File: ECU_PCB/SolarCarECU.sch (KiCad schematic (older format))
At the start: 123 parts, among them J1 Screw_Terminal_01x02, J2 USB_B, J3 Screw_Terminal_01x05, J4 Screw_Terminal_01x08, J5 Screw_Terminal_01x08, J6 Screw_Terminal_01x14, J7 Screw_Terminal_01x14, Q1 QM6015D, Q2 PZT2222A, Q3 QM6015D, Q4 QM6015D, Q5 QM6015D, Q6 QM6015D, U1 Teensy3.6, U10 LM324A, U2 EL7202CN, U3 EL7202CN, U4 L7805, U5 MCP2562-E-P, U6 MCP2562-E-P, U7 4504, U8 4504, U9 4504

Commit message: fixed UART_1_* pins, added LV_KILL_SENSE, added *STEER_CTRL*
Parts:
- added C41: C, Capacitor_SMD:C_0603_1608Metric, symbol SolarCarECU-rescue:C-Device-SolarCarECU-rescue
- added D10, D3, D4, D5, D6, D7, D8, D9: D, Diode_SMD:D_SOD-123, symbol Device:D
- added R58, R59: R, Resistor_SMD:R_0603_1608Metric, symbol SolarCarECU-rescue:R-Device-SolarCarECU-rescue
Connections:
- net labels added: LV_STEER_CTRL, STEER_CTRL
- net labels removed: UART_RX, UART_TX
- wire segments 576 -> 618
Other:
- moved on the sheet: C21, C30, C35, C37, C38, C39, C40, R12, R13, R18, R19, R28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

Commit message: reworked PCB and fixed all issues brought up
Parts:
- removed BT1: Battery_Cell, Battery:BatteryHolder_Keystone_1060_1x2032, symbol Device:Battery_Cell
- removed C4: 470uF, Capacitor_THT:CP_Radial_D13.0mm_P5.00mm, symbol SolarCarECU-rescue:CP-Device-SolarCarECU-rescue
- removed D1: D_Schottky, Diode_SMD:D_SOD-123, symbol SolarCarECU-rescue:D_Schottky-Device-SolarCarECU-rescue
- removed D2: D_Zener, Diode_SMD:D_SOD-123, symbol SolarCarECU-rescue:D_Zener-Device-SolarCarECU-rescue
- removed J1: Screw_Terminal_01x02, Connector_Phoenix_MC_HighVoltage:PhoenixContact_MCV_1,5_2-G-5.08_1x02_P5.08mm_Vertical, symbol SolarCarECU-rescue:Screw_Terminal_01x02-Connector-SolarCarECU-rescue
- removed J2: USB_B, Connector_USB:USB_B_OST_USB-B1HSxx_Horizontal, symbol Connector:USB_B
- removed J3: Screw_Terminal_01x05, Connector_Phoenix_MC_HighVoltage:PhoenixContact_MCV_1,5_5-G-5.08_1x05_P5.08mm_Vertical, symbol Connector:Screw_Terminal_01x05
- removed J4, J5: Screw_Terminal_01x08, Connector_PinSocket_2.54mm:PinSocket_1x08_P2.54mm_Vertical, symbol SolarCarECU-rescue:Screw_Terminal_01x08-Connector-SolarCarECU-rescue
- removed J6, J7: Screw_Terminal_01x14, Connector_PinSocket_2.54mm:PinSocket_1x14_P2.54mm_Vertical, symbol SolarCarECU-rescue:Screw_Terminal_01x14-Connector-SolarCarECU-rescue
- removed Q2: PZT2222A, Package_TO_SOT_SMD:SOT-223, symbol SolarCarECU-rescue:PZT2222A-Transistor_BJT-SolarCarECU-rescue
- removed R43: 0, Resistor_SMD:R_1206_3216Metric, symbol SolarCarECU-rescue:R-Device-SolarCarECU-rescue
- removed R7: 120, Resistor_SMD:R_0603_1608Metric, symbol SolarCarECU-rescue:R-Device-SolarCarECU-rescue
- added C2: 470uF, Capacitor_THT:CP_Radial_D13.0mm_P5.00mm, symbol SolarCarECU-rescue:CP-Device-SolarCarECU-rescue
- added C7: 100n, Capacitor_SMD:C_1206_3216Metric, symbol SolarCarECU-rescue:C-Device-SolarCarECU-rescue
- added C8: 4.7u, Capacitor_SMD:C_1206_3216Metric, symbol SolarCarECU-rescue:C-Device-SolarCarECU-rescue
- added D1: 599-0210, LED_SMD:LED_1206_3216Metric, symbol Device:LED
- added D12, D13, D6, D7: D, Diode_SMD:D_SOD-123, symbol SolarCarECU-rescue:D-Device
- added D16: 599-0291, LED_SMD:LED_1206_3216Metric, symbol Device:LED
- added D2: D_Zener, Diode_SMD:D_SOD-123, symbol Device:D_Zener
- added D3: 599-0230, LED_SMD:LED_1206_3216Metric, symbol Device:LED
- added J2: Screw_Terminal_01x08, Connector_Phoenix_MC_HighVoltage:PhoenixContact_MCV_1,5_8-G-5.08_1x08_P5.08mm_Vertical, symbol Connector:Screw_Terminal_01x08
- added J3, J4, J5, J6, J7, J8: Screw_Terminal_01x08, Connector_PinSocket_2.54mm:PinSocket_1x08_P2.54mm_Vertical, symbol Connector:Screw_Terminal_01x08
- added Q4, Q5: QM6015D, Package_TO_SOT_SMD:TO-252-2, symbol SolarCarECU-rescue:QM6015D-Transistor_FET-SolarCarECU-rescue
- added R43, R7: 4.7, Resistor_SMD:R_0603_1608Metric, symbol SolarCarECU-rescue:R-Device
- added R6, R61, R62: 1k, Resistor_SMD:R_1206_3216Metric, symbol SolarCarECU-rescue:R-Device-SolarCarECU-rescue
- added U11: MCP1403, Package_DIP:DIP-8_W7.62mm, symbol SolarCarECU-rescue:EL7202CN-Driver_FET-SolarCarECU-rescue
- C10: renamed from C3; value 0.47u -> 100n; footprint Capacitor_SMD:C_0603_1608Metric -> Capacitor_SMD:C_1206_3216Metric
- C11: renamed from C6; footprint Capacitor_SMD:C_0603_1608Metric -> Capacitor_SMD:C_1206_3216Metric
- C12: renamed from C8; footprint Capacitor_SMD:C_0603_1608Metric -> Capacitor_SMD:C_1206_3216Metric
- C13: renamed from C11; value 0.47u -> 100n; footprint Capacitor_SMD:C_0603_1608Metric -> Capacitor_SMD:C_1206_3216Metric
- C14: renamed from C12; value 0.47u -> 100n; footprint Capacitor_SMD:C_0603_1608Metric -> Capacitor_SMD:C_1206_3216Metric
- C15: renamed from C13; value 0.47u -> 100n; footprint Capacitor_SMD:C_0603_1608Metric -> Capacitor_SMD:C_1206_3216Metric
- C16: renamed from C14; value 0.47u -> 100n; footprint Capacitor_SMD:C_0603_1608Metric -> Capacitor_SMD:C_1206_3216Metric
- C17: renamed from C15; value 0.47u -> 100n; footprint Capacitor_SMD:C_0603_1608Metric -> Capacitor_SMD:C_1206_3216Metric
- C18: renamed from C16; value 0.47u -> 100n; footprint Capacitor_SMD:C_0603_1608Metric -> Capacitor_SMD:C_1206_3216Metric
- C19: renamed from C17; value 0.47u -> 100n; footprint Capacitor_SMD:C_0603_1608Metric -> Capacitor_SMD:C_1206_3216Metric
- C20: renamed from C18; footprint Capacitor_SMD:C_0603_1608Metric -> Capacitor_SMD:C_1206_3216Metric
- C21, C30, C35, C37, C38, C39, C40, C41: value C -> 1n
- C3: renamed from C10; footprint Capacitor_THT:CP_Radial_D13.0mm_P5.00mm -> Capacitor_SMD:C_1206_3216Metric
- C36: renamed from C19; footprint Capacitor_SMD:C_0603_1608Metric -> Capacitor_SMD:C_1206_3216Metric
- C4: renamed from C2; value 0.47u -> 100n; footprint Capacitor_SMD:C_0603_1608Metric -> Capacitor_SMD:C_1206_3216Metric
- C42: renamed from C20; footprint Capacitor_SMD:C_0603_1608Metric -> Capacitor_SMD:C_1206_3216Metric
- C43: renamed from C36; value 0.47u -> 100n; footprint Capacitor_SMD:C_0603_1608Metric -> Capacitor_SMD:C_1206_3216Metric
- C5: footprint Capacitor_SMD:C_0603_1608Metric -> Capacitor_SMD:C_1206_3216Metric
- C6: renamed from C7; footprint Capacitor_SMD:C_0603_1608Metric -> Capacitor_SMD:C_1206_3216Metric
- C9: value 10uF -> 47u; footprint Capacitor_SMD:C_0603_1608Metric -> Capacitor_SMD:C_1206_3216Metric
- D10: renamed from D7; symbol Device:D -> SolarCarECU-rescue:D-Device
- D11: renamed from D8; symbol Device:D -> SolarCarECU-rescue:D-Device
- D14: renamed from D9; symbol Device:D -> SolarCarECU-rescue:D-Device
- D15: renamed from D10; symbol Device:D -> SolarCarECU-rescue:D-Device
- D4: renamed from D3; symbol Device:D -> SolarCarECU-rescue:D-Device
- D5: renamed from D4; symbol Device:D -> SolarCarECU-rescue:D-Device
- D8: renamed from D5; symbol Device:D -> SolarCarECU-rescue:D-Device
- D9: renamed from D6; symbol Device:D -> SolarCarECU-rescue:D-Device
- R1, R10, R11, R2, R3, R4, R52, R53, R8, R9: footprint Resistor_SMD:R_0603_1608Metric -> Resistor_SMD:R_1206_3216Metric
- R12, R18, R28, R30, R40, R44, R46, R58: value R -> 1M
- R13, R19, R29, R31, R41, R45, R47, R59: value R -> 330k
- R48, R49, R50, R51: symbol Device:R -> SolarCarECU-rescue:R-Device
- R60: renamed from R6; footprint Resistor_SMD:R_0603_1608Metric -> Resistor_SMD:R_1206_3216Metric
- U2, U3: value EL7202CN -> MCP1403
- renumbered Q3 to Q2, Q5 to Q3, Q4 to Q6, Q6 to Q7
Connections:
- net labels added: +VDC, LEFT_BLINKERS, LV_LEFT_BLINKERS, LV_RIGHT_BLINKERS, LV_STROBE, RIGHT_BLINKERS, STROBE
- net labels removed: BLINKERS, LV_BLINKERS, USB_MASTER-SLAVE_SEL
- wire segments 618 -> 663
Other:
- note removed: "This resistor is for debugging.\nIt can be removed it to disconnect\n12V from everything else."
- moved on the sheet: C1, C10, C11, C12, C13, C14, C15, C16, C17, C18, C19, C20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

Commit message: added HORN_CTRL and fixed silkscreen issues
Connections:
- net GND: no longer U7.14 (Fin)
- net HAZARD_LED: no longer J6.8 (Pin_8)
- net LV_HORN_CTRL: now reaches U1.49 (22_A8_PWM_Touch)
- net LV_HORN_CTRL: now also U7.15 (Fout)
- new net HORN_CTRL: J6.8 (Pin_8), U7.14 (Fin)
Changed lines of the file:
@@
 Wire Wire Line
 	10700 2600 11400 2600
-Wire Wire Line
-	10700 3000 10950 3000
 $Comp
 L SolarCarECU-rescue:+12V-power-SolarCarECU-rescue #PWR0139
@@
 Text Label 20450 7450 0    50   ~ 0
 KILL_SENSE
-Text Label 20450 7550 0    50   ~ 0
-HAZARD_LED
 Text Label 20450 3450 0    50   ~ 0
 BRAKELIGHTS
@@
 Connection ~ 3450 2700
 Wire Wire Line
-	10950 3200 10950 3000
-Connection ~ 10950 3200
-Wire Wire Line
 	21100 8200 21250 8200
 Text Label 20450 3250 0    50   ~ 0
@@
 Wire Wire Line
 	3450 1400 4150 1400
+Text Label 11400 3000 2    50   ~ 0
+HORN_CTRL
+Text Label 9700 3000 2    50   ~ 0
+LV_HORN_CTRL
+Wire Wire Line
+	9700 3000 9800 3000
+Text Label 5450 14250 0    50   ~ 0
+LV_HORN_CTRL
+Wire Wire Line
+	5400 14250 5450 14250
+Wire Wire Line
+	10700 3000 11400 3000
+Text Label 20450 7550 0    50   ~ 0
+HORN_CTRL
 $EndSCHEMATC

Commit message: added HEADLIGHT_CTRL pin but had to sacrifice a 12V output for it.
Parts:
- added C44: 1n, Capacitor_SMD:C_0603_1608Metric, symbol SolarCarECU-rescue:C-Device-SolarCarECU-rescue
- added R63: 1M, Resistor_SMD:R_0603_1608Metric, symbol SolarCarECU-rescue:R-Device-SolarCarECU-rescue
- added R64: 330k, Resistor_SMD:R_0603_1608Metric, symbol SolarCarECU-rescue:R-Device-SolarCarECU-rescue
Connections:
- net +12V: no longer J6.1 (Pin_1)
- net GNDA: now also J6.1 (Pin_1), C44.2, R64.2; no longer J6.2 (Pin_2)
- net LV_HEADLIGHT_CTRL: now reaches U1.50 (23_A9_PWM_Touch)
- net LV_HEADLIGHT_CTRL: now also C44.1, R63.2, R64.1
- new net HEADLIGHT_CTRL: J6.2 (Pin_2), R63.1
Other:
- moved on the sheet: R12, R18, R28, R30, R40, R44, R46, R58

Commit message: schema update
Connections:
- net LV_STROBE: now also U1.8 (6_PWM)
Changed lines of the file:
@@
 EESchema Schematic File Version 4
 LIBS:SolarCarECU-cache
-EELAYER 29 0
+EELAYER 26 0
 EELAYER END
 $Descr A2 23386 16535
@@
 Wire Wire Line
 	5400 14150 5450 14150
+Text Label 2900 11250 2    50   ~ 0
+LV_STROBE
+Wire Wire Line
+	2900 11250 3400 11250
 $EndSCHEMATC

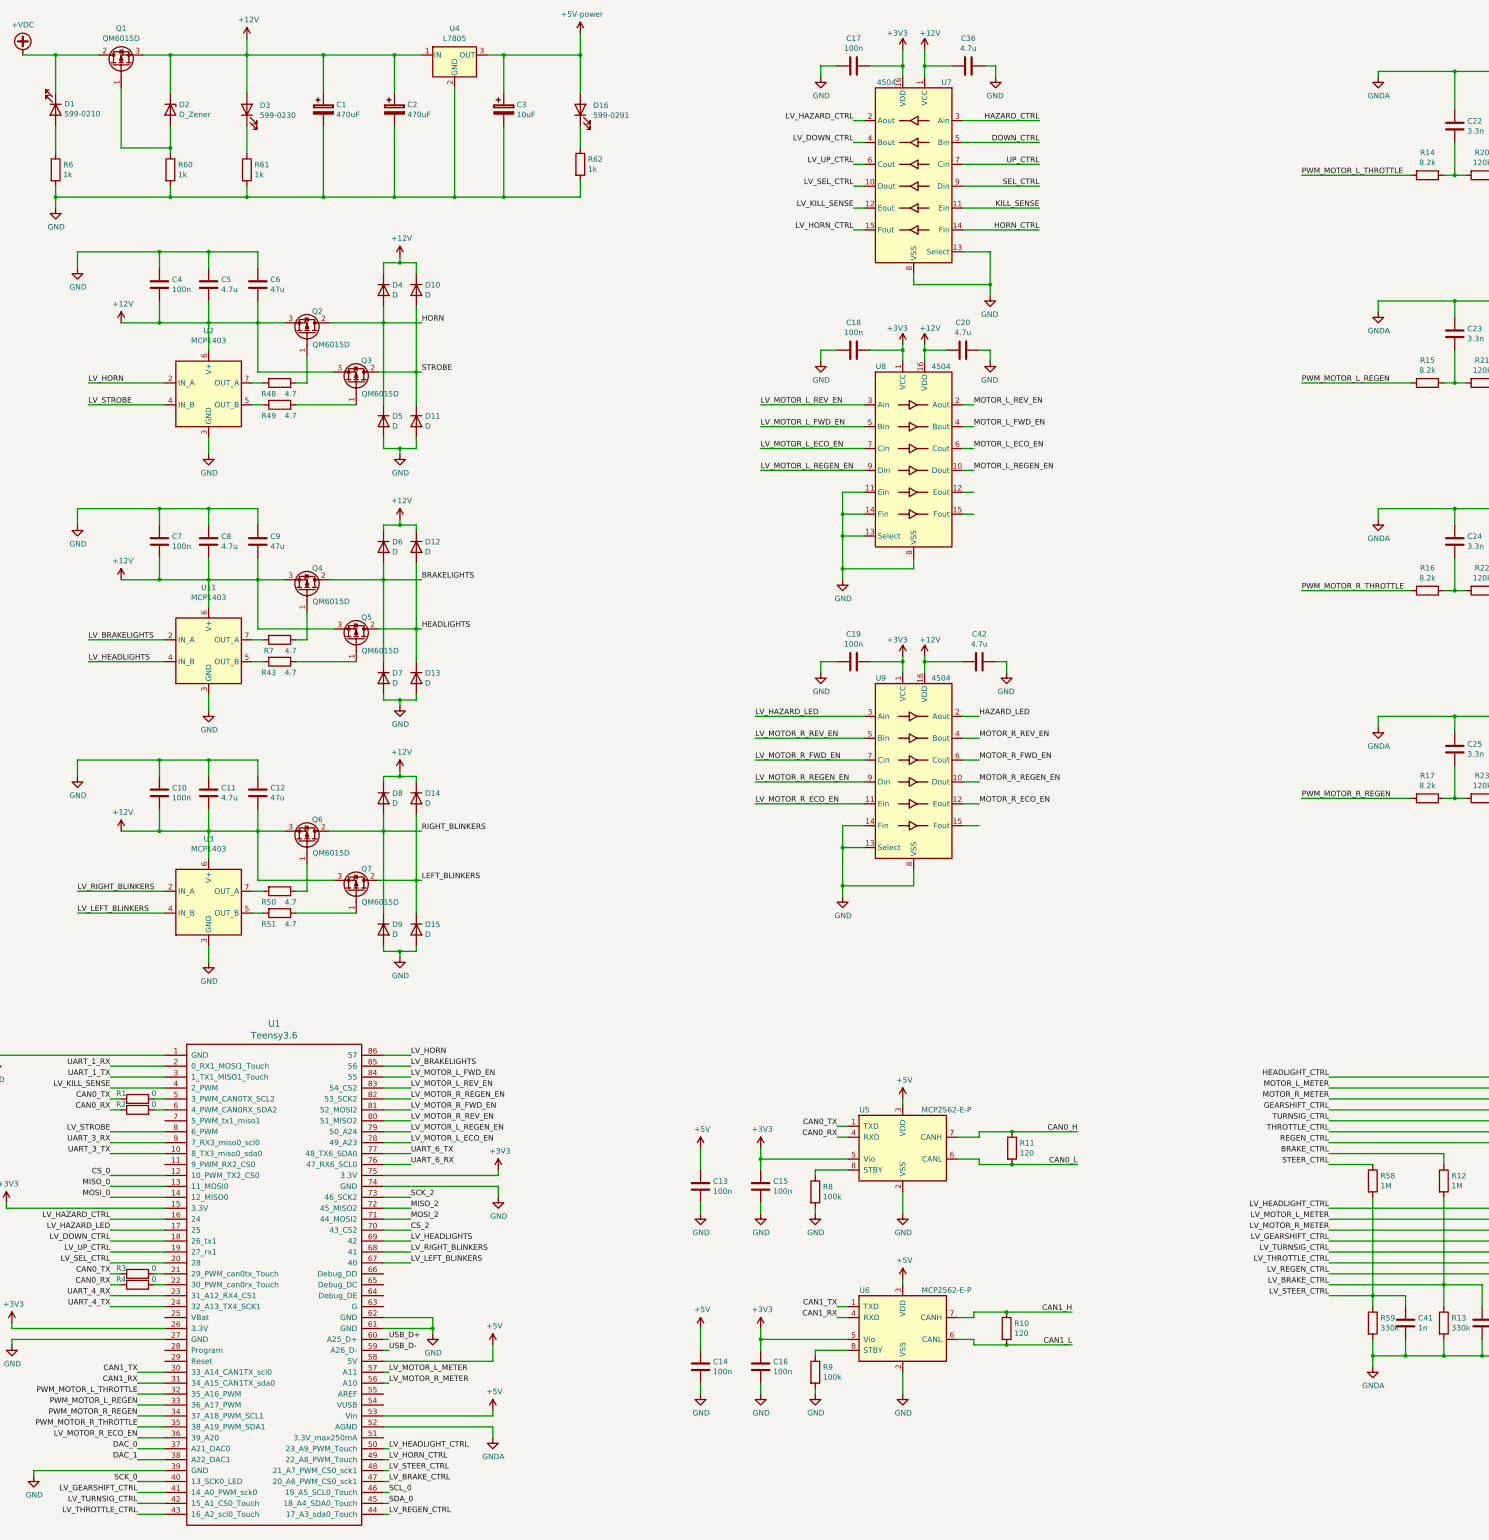
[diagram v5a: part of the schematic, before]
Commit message: added pulldown resistors to schematic. No PCB edits done.
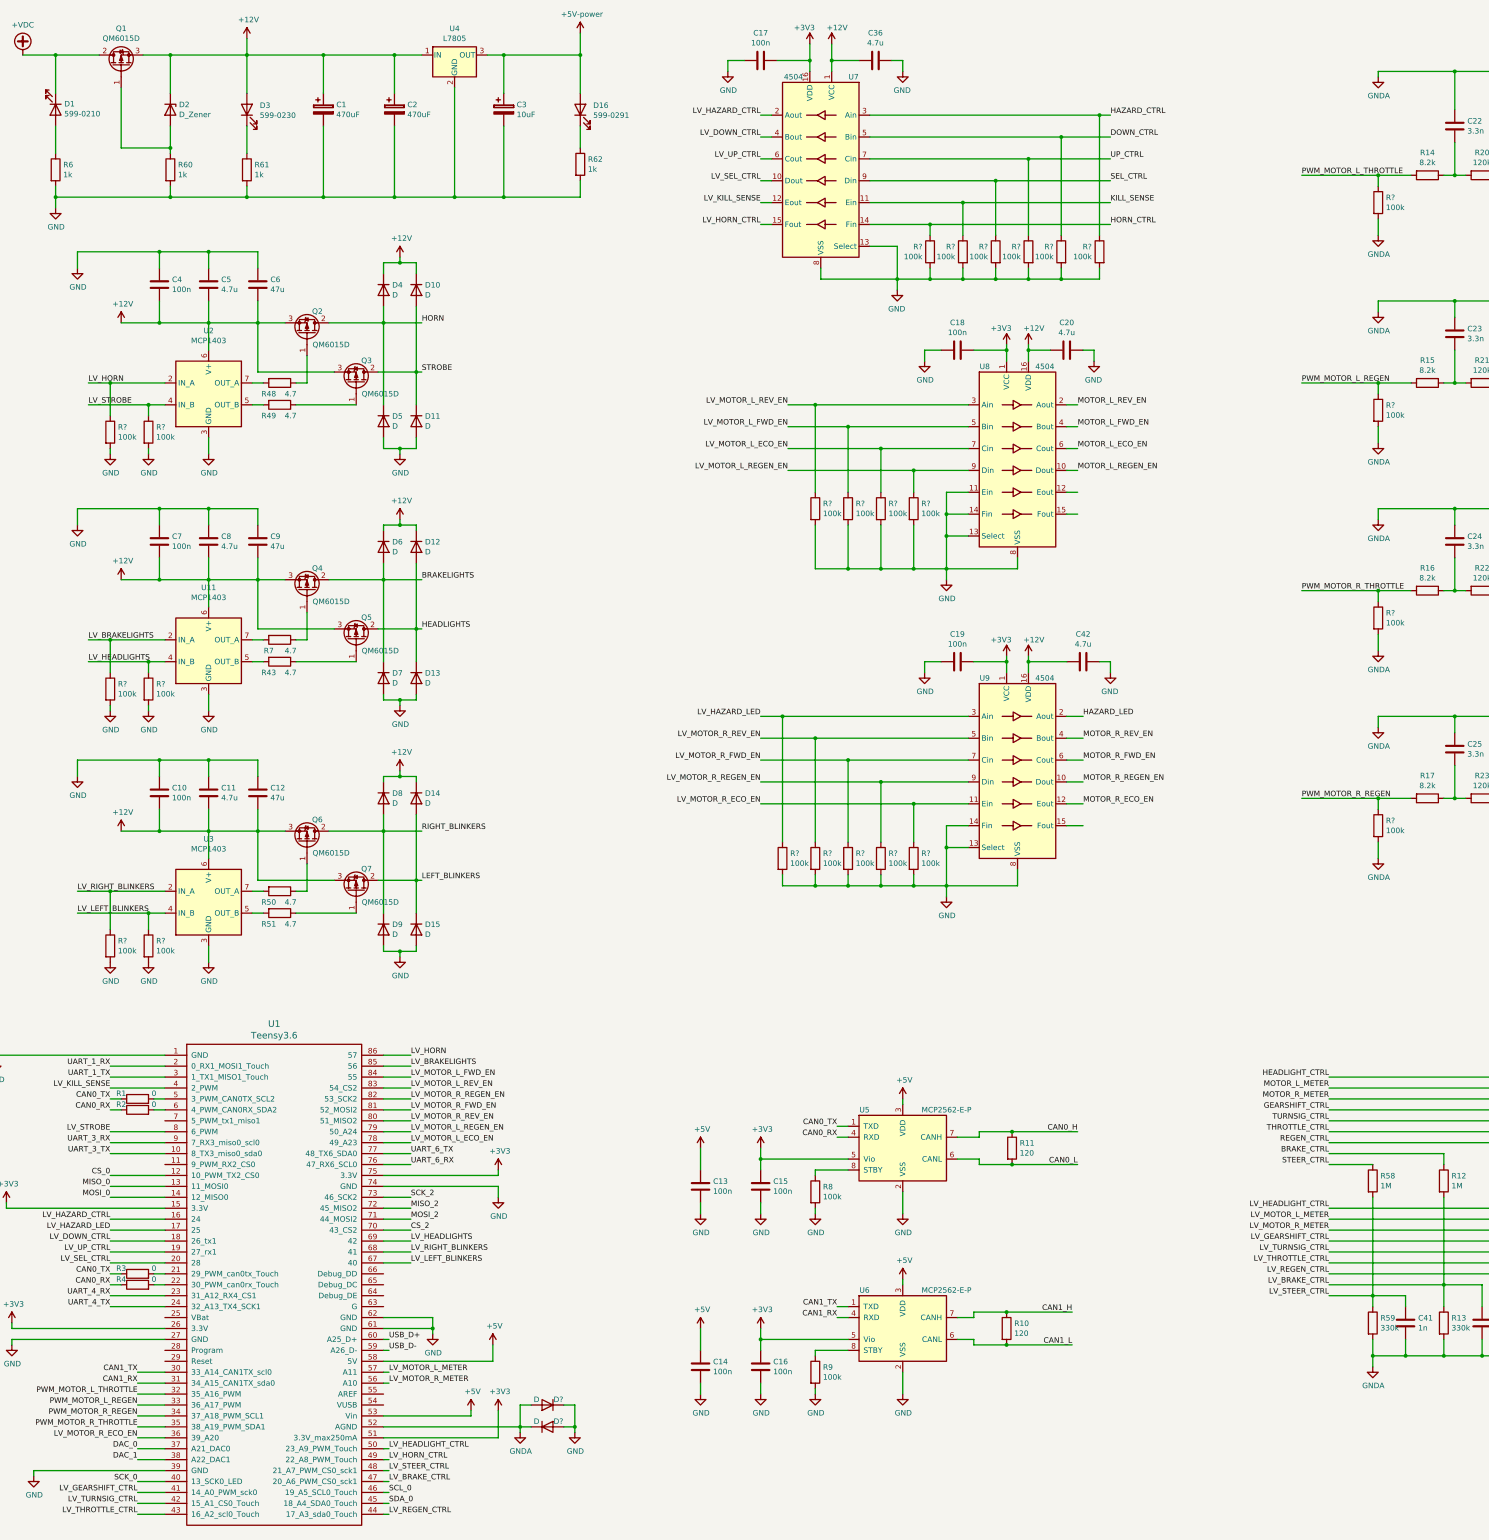
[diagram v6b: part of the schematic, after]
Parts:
- added D? (x2): D, Diode_SMD:D_SOD-123, symbol Device:D
- added R? (x25): 100k, Resistor_SMD:R_1206_3216Metric, symbol SolarCarECU-rescue:R-Device-SolarCarECU-rescue
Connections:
- net +3V3: now also U1.51 (3.3V_max250mA)
- net DOWN_CTRL: now also R?.1
- net GND: now also D?.1 (K), D?.2 (A), R?.2, R?.2, R?.2, R?.2, R?.2, R?.2, R?.2, R?.2, R?.2, R?.2, R?.2, R?.2, R?.2, R?.2, R?.2, R?.2, R?.2, R?.2, R?.2, R?.2, R?.2
- net GNDA: now also D?.1 (K), D?.2 (A), R?.2, R?.2, R?.2, R?.2
- net HAZARD_CTRL: now also R?.1
- net HORN_CTRL: now also R?.1
- net KILL_SENSE: now also R?.1
- net LV_BRAKELIGHTS: now also R?.1
- net LV_HAZARD_LED: now also R?.1
- net LV_HEADLIGHTS: now also R?.1
- net LV_HORN: now also R?.1
- net LV_LEFT_BLINKERS: now also R?.1
- net LV_MOTOR_L_ECO_EN: now also R?.1
- net LV_MOTOR_L_FWD_EN: now also R?.1
- net LV_MOTOR_L_REGEN_EN: now also R?.1
- net LV_MOTOR_L_REV_EN: now also R?.1
- net LV_MOTOR_R_ECO_EN: now also R?.1
- net LV_MOTOR_R_FWD_EN: now also R?.1
- net LV_MOTOR_R_REGEN_EN: now also R?.1
- net LV_MOTOR_R_REV_EN: now also R?.1
- net LV_RIGHT_BLINKERS: now also R?.1
- net LV_STROBE: now also R?.1
- net PWM_MOTOR_L_REGEN: now also R?.1
- net PWM_MOTOR_L_THROTTLE: now also R?.1
- net PWM_MOTOR_R_REGEN: now also R?.1
- net PWM_MOTOR_R_THROTTLE: now also R?.1
- net SEL_CTRL: now also R?.1
- net UP_CTRL: now also R?.1
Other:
- moved on the sheet: C17, C18, C19, C20, C36, C42, U7, U8, U9
